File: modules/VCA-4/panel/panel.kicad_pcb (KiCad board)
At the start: 2 copper layers, 50.5 x 128.5 mm, 24 parts

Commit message: VCA-4: tweak front panel - wip
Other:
- board text added: "TODO: holes 6.3 & 7.3 mm"
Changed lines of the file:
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@@
     (pad "" np_thru_hole circle locked (at 0 0) (size 6.3 6.3) (drill 6.3) (layers *.Cu *.Mask))
   )
+  (gr_circle (center 159.295 66.047) (end 168.545 66.047) (layer "Dwgs.User") (width 0.1) (fill none))
+  (gr_circle (center 159.295 85.097) (end 168.545 85.097) (layer "Dwgs.User") (width 0.1) (fill none))
   (gr_line (start 119.999989 178.499999) (end 119.999989 50.000002) (layer "Edge.Cuts") (width 0.1524))
   (gr_line (start 170.499989 50.000002) (end 170.499989 178.499999) (layer "Edge.Cuts") (width 0.1524))
   (gr_line (start 119.999989 50.000002) (end 170.499989 50.000002) (layer "Edge.Cuts") (width 0.1524))
   (gr_line (start 170.499989 178.499999) (end 119.999989 178.499999) (layer "Edge.Cuts") (width 0.1524))
+  (gr_text "TODO: holes 6.3 & 7.3 mm" (at 156.591 97.409) (layer "Cmts.User")
+    (effects (font (size 1 1) (thickness 0.15)))
+  )
   (zone (net 0) (net_name "") (layer "F.Cu") (hatch edge 0.508)
     (connect_pads (clearance 0.2032))

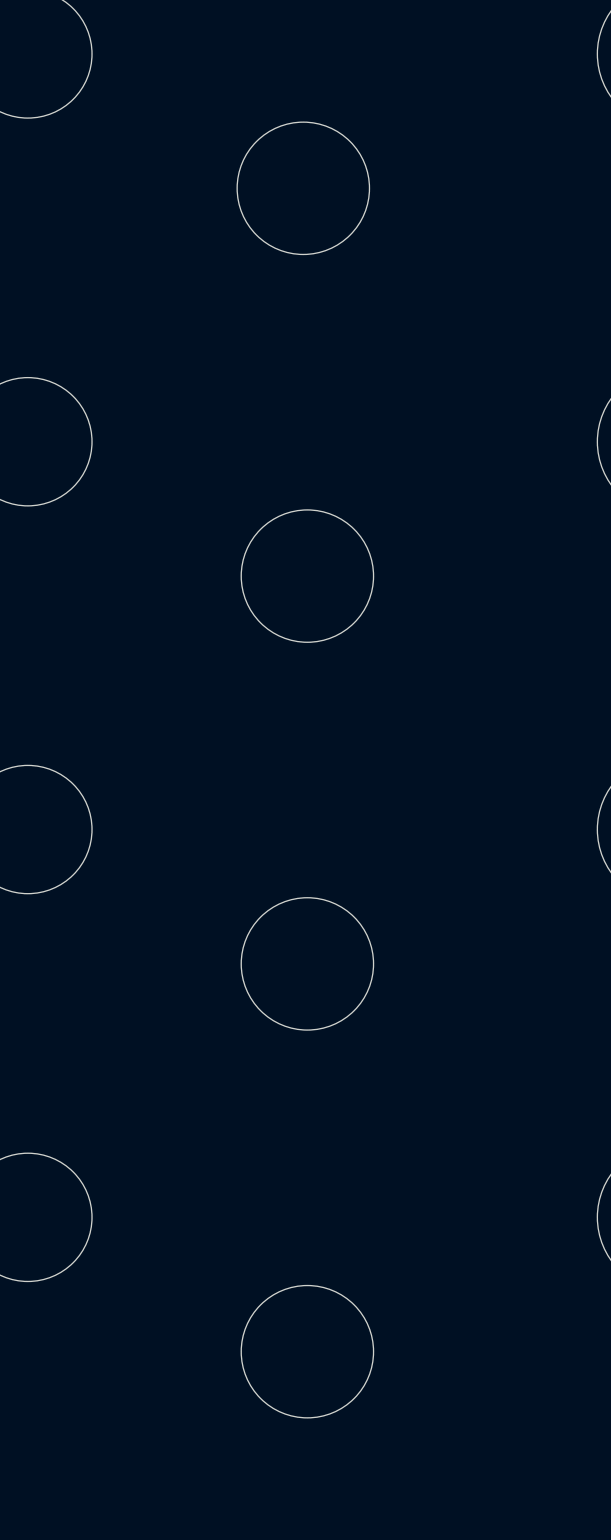
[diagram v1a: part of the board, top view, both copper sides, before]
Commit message: VCA-4: front panel: adjust some hole sizes
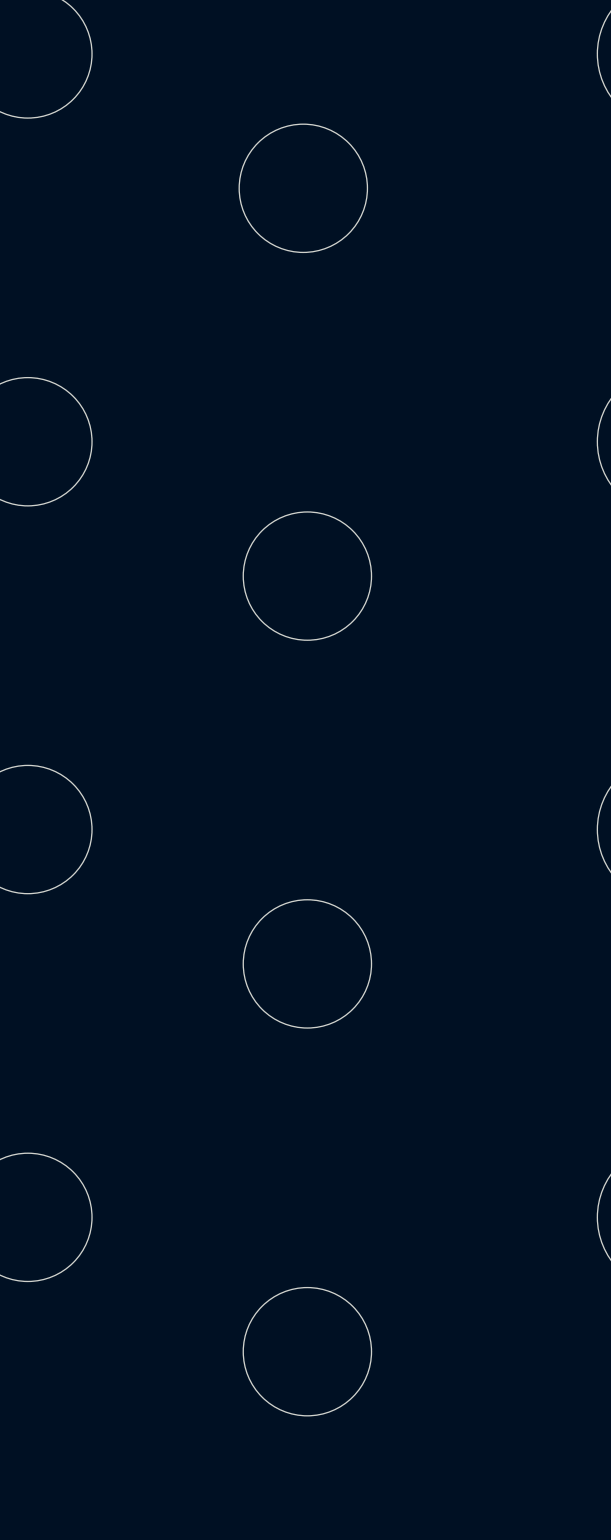
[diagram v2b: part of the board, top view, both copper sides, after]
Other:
- board text removed: "TODO: holes 6.3 & 7.3 mm"
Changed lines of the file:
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@@
       (effects (font (size 1 1) (thickness 0.15)))
     )
-    (pad "" np_thru_hole circle (at 0 0) (size 6.5 6.5) (drill 6.5) (layers F&B.Cu *.Mask))
+    (pad "" np_thru_hole circle (at 0 0) (size 6.3 6.3) (drill 6.3) (layers F&B.Cu *.Mask))
   )
   (footprint "-lmp-holes:MountingHole_Jack_3.5mm_PJ398" (layer "F.Cu")
@@
       (effects (font (size 1 1) (thickness 0.15)))
     )
-    (pad "" np_thru_hole circle (at 0 0) (size 6.5 6.5) (drill 6.5) (layers F&B.Cu *.Mask))
+    (pad "" np_thru_hole circle (at 0 0) (size 6.3 6.3) (drill 6.3) (layers F&B.Cu *.Mask))
   )
   (footprint "-lmp-holes:MountingHole_Jack_3.5mm_PJ398" (layer "F.Cu")
@@
       (effects (font (size 1 1) (thickness 0.15)))
     )
-    (pad "" np_thru_hole circle (at 0 0) (size 6.5 6.5) (drill 6.5) (layers F&B.Cu *.Mask))
+    (pad "" np_thru_hole circle (at 0 0) (size 6.3 6.3) (drill 6.3) (layers F&B.Cu *.Mask))
   )
   (footprint "-lmp-holes:MountingHole_Pot_SongHuei" (layer "F.Cu")
@@
       (effects (font (size 1 1) (thickness 0.15)))
     )
-    (pad "" np_thru_hole circle (at 0 0) (size 6.5 6.5) (drill 6.5) (layers F&B.Cu *.Mask))
+    (pad "" np_thru_hole circle (at 0 0) (size 6.3 6.3) (drill 6.3) (layers F&B.Cu *.Mask))
   )
   (footprint "-lmp-holes:MountingHole_Jack_3.5mm_PJ398" (layer "F.Cu")
@@
     (pad "" np_thru_hole circle locked (at 0 0) (size 6.3 6.3) (drill 6.3) (layers *.Cu *.Mask))
   )
-  (gr_circle (center 159.295 66.047) (end 168.545 66.047) (layer "Dwgs.User") (width 0.1) (fill none))
-  (gr_circle (center 159.295 85.097) (end 168.545 85.097) (layer "Dwgs.User") (width 0.1) (fill none))
   (gr_line (start 119.999989 178.499999) (end 119.999989 50.000002) (layer "Edge.Cuts") (width 0.1524))
   (gr_line (start 170.499989 50.000002) (end 170.499989 178.499999) (layer "Edge.Cuts") (width 0.1524))
   (gr_line (start 119.999989 50.000002) (end 170.499989 50.000002) (layer "Edge.Cuts") (width 0.1524))
   (gr_line (start 170.499989 178.499999) (end 119.999989 178.499999) (layer "Edge.Cuts") (width 0.1524))
-  (gr_text "TODO: holes 6.3 & 7.3 mm" (at 156.591 97.409) (layer "Cmts.User")
-    (effects (font (size 1 1) (thickness 0.15)))
-  )
   (zone (net 0) (net_name "") (layer "F.Cu") (hatch edge 0.508)
     (connect_pads (clearance 0.2032))

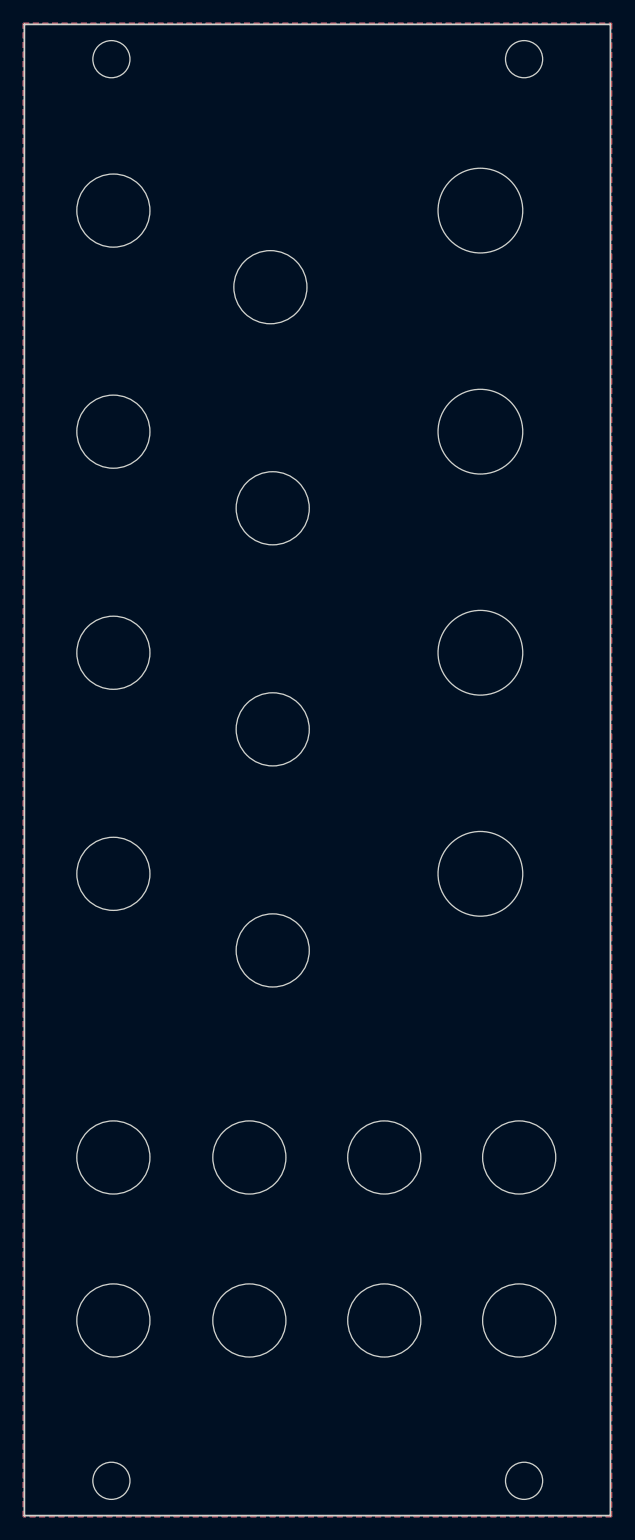
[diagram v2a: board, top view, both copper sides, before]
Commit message: VCA-4: front panel adjustments
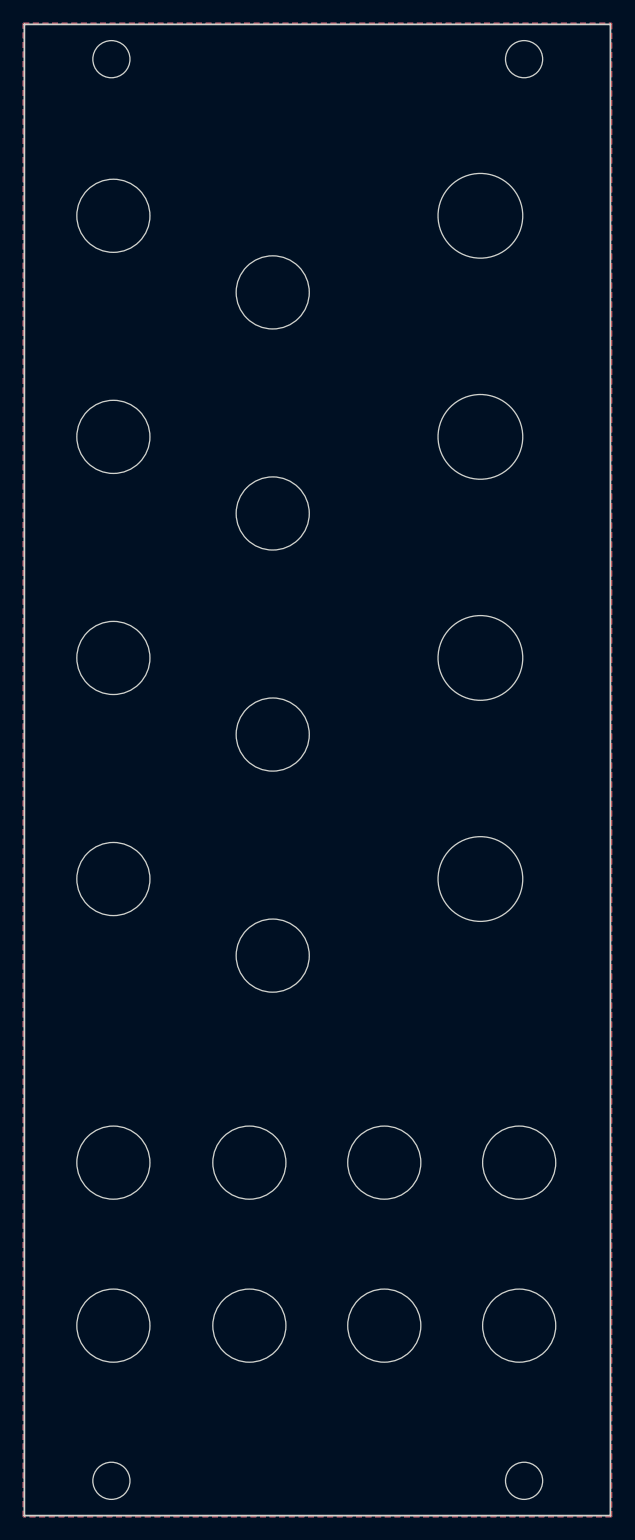
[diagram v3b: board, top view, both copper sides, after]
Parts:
- moved REF** 0.49 mm to (141.4, 73.1)
- moved REF** 0.45 mm to (127.7, 85.5)
- moved REF** 0.45 mm to (141.4, 130.2)
- moved REF** 0.45 mm to (127.7, 66.5)
- moved REF** 0.45 mm to (159.3, 85.5)
- moved REF** 0.45 mm to (159.3, 66.5)
- moved REF** 0.45 mm to (159.3, 104.6)
- moved REF** 0.45 mm to (127.7, 104.6)
- moved REF** 0.45 mm to (141.4, 92.1)
- moved REF** 0.45 mm to (141.4, 111.2)
- moved REF** 0.45 mm to (127.7, 123.6)
- moved REF** 0.45 mm to (159.3, 123.6)
- moved REF** 0.44 mm to (162.6, 162.1)
- moved REF** 0.44 mm to (151.0, 162.1)
- moved REF** 0.44 mm to (127.7, 162.1)
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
